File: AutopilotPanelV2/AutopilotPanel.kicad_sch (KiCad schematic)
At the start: 142 parts, among them J1 USB_C_Receptacle_USB2.0_16P, J2 PINHD_1x2_Male, J3 PINHD_1x2_Male, J4 PINHD_1x2_Male, J5 PINHD_1x2_Male, J6 PINHD_1x2_Male, J7 PINHD_1x2_Male, Q1 NFET-SOT23, Q2 NFET-SOT23, Q3 NFET-SOT23, Q4 NFET-SOT23, Q5 NFET-SOT23, Q6 NFET-SOT23, SW1 SW_SPST_Tactile_6x6, SW10 SW_SPST_Tactile_6x6, SW11 SW_SPST_Tactile_6x6, SW12 SW_SPST_Tactile_6x6, SW13 SW_SPST_Tactile_6x6, SW14 SW_SPST_Tactile_6x6, SW15 RotaryEncoder_Switch_EC11E, SW2 SW_SPST_Tactile_6x6, SW3 SW_SPST_Tactile_6x6, SW4 SW_SPST_Tactile_6x6, SW5 SW_SPST_Tactile_6x6, SW6 SW_SPST_Tactile_6x6, SW7 SW_SPST_Tactile_6x6, SW8 SW_SPST_Tactile_6x6, SW9 SW_SPST_Tactile_6x6, U1 74HC164, U10 7SegmentFJ5161AH, U11 7SegmentFJ5161AH, U12 7SegmentFJ5161AH, U13 7SegmentFJ5161AH, U14 7SegmentFJ5161AH, U16 TPS62160DSG, U2 74HC164, U3 74HC164, U4 74HC164, U5 74HC164, U6 74HC164, U7 74HC164, U8 74HC164, U9 7SegmentFJ5161AH

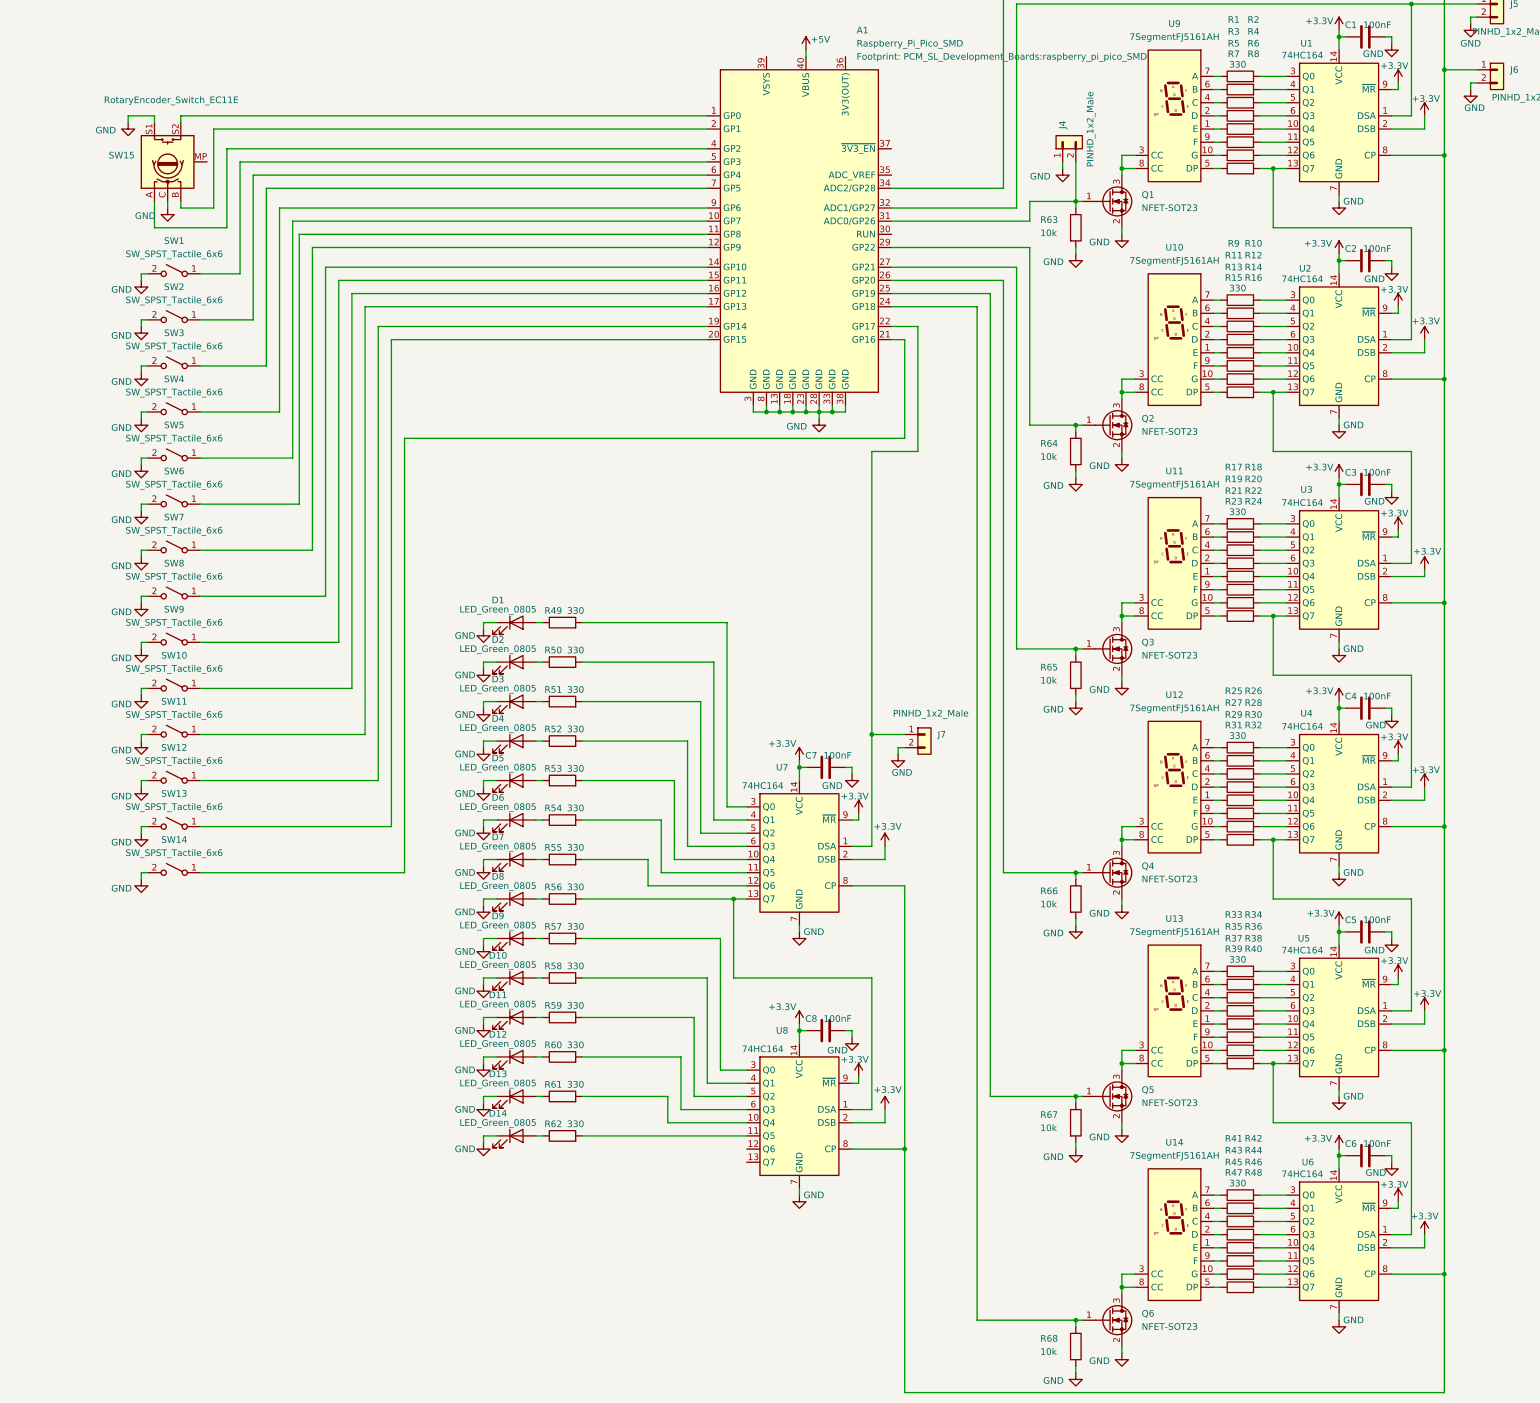
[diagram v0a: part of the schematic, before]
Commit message: Added 74HC165 to read buttons in schematic
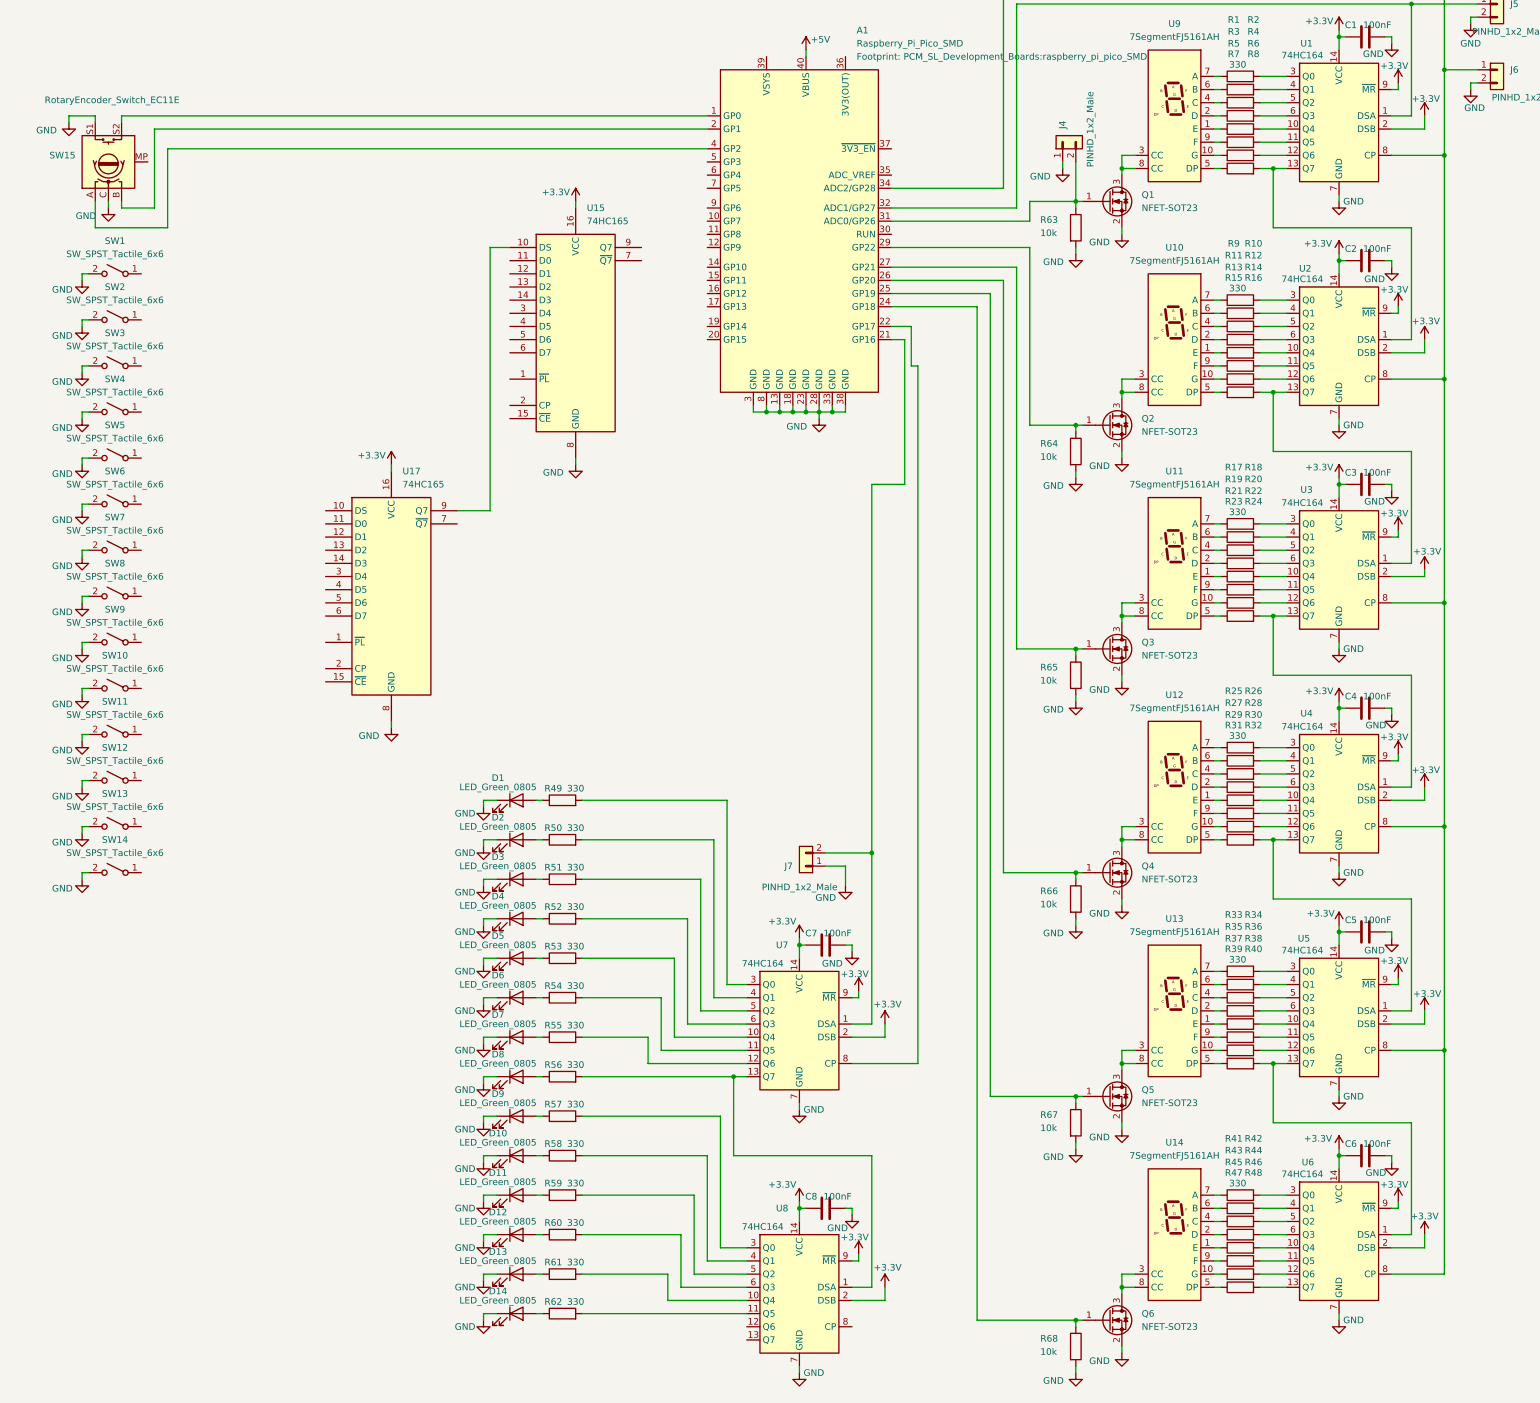
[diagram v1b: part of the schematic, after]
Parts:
- added U15, U17: 74HC165, symbol 74xx:74HC165
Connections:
- net +3.3V: now also U15.16 (VCC), U17.16 (VCC)
- net GND: now also J7.1, U15.8 (GND), U17.8 (GND); no longer J7.2
- net at SW1.1 (A): no longer A1.5 (GP3)
- net at A1.34 (ADC2/GP28), J6.1, U1.8 (CP)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: no longer U7.8 (CP), U8.8 (CP)
- net at SW11.1 (A): no longer A1.17 (GP13)
- net at SW7.1 (A): no longer A1.12 (GP9)
- net at SW12.1 (A): no longer A1.19 (GP14)
- net at SW2.1 (A): no longer A1.6 (GP4)
- net at SW9.1 (A): no longer A1.15 (GP11)
- net at SW8.1 (A): no longer A1.14 (GP10)
- net at SW10.1 (A): no longer A1.16 (GP12)
- net at SW13.1 (A): no longer A1.20 (GP15)
- net at A1.10 (GP7): no longer SW5.1 (A)
- net at A1.11 (GP8): no longer SW6.1 (A)
- net at A1.21 (GP16): now also J7.2, U7.1 (DSA); no longer SW14.1 (A)
- net at A1.7 (GP5): no longer SW3.1 (A)
- net at A1.9 (GP6): no longer SW4.1 (A)
- new net: A1.22 (GP17), U7.8 (CP)
- new net: U15.10 (DS), U17.9 (Q7)
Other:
- moved on the sheet: C7, C8, D1, D10, D11, D12, D13, D14, D2, D3, D4, D5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
